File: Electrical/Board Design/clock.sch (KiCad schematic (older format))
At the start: 40 parts, among them CON1 AVR-ISP-6, IC1 ATTINY84A-SS, Q1 FET_N, Q2 FET_P, SW1 SPST, U1 MCP1624, X1 CRYSTAL 32.768kHz

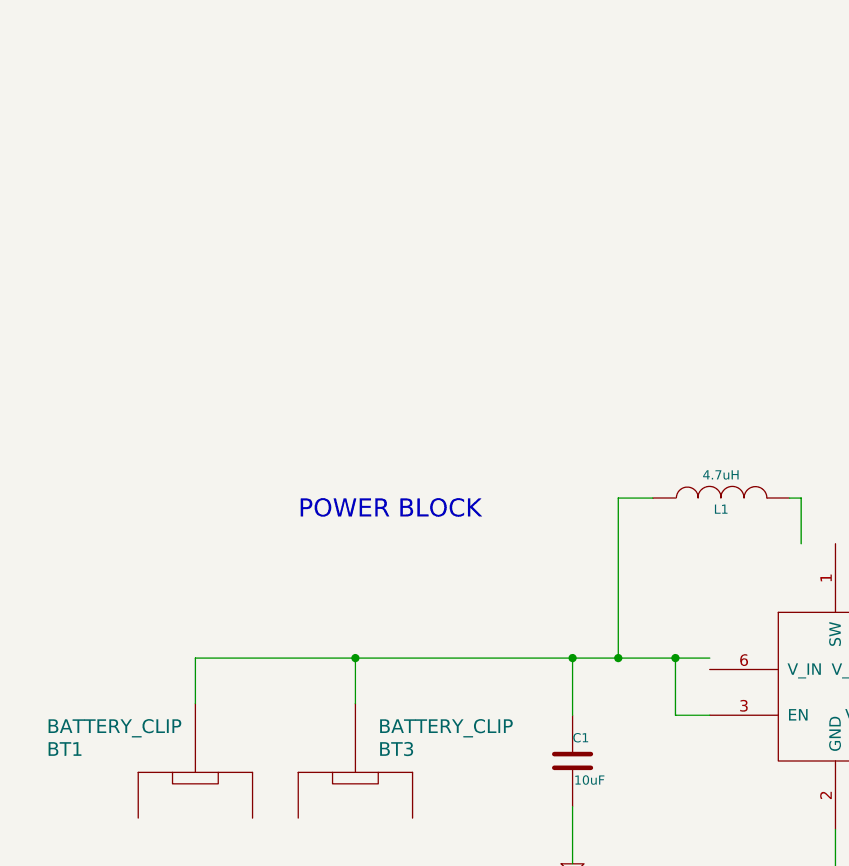
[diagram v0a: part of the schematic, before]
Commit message: added LDO to schematic and board
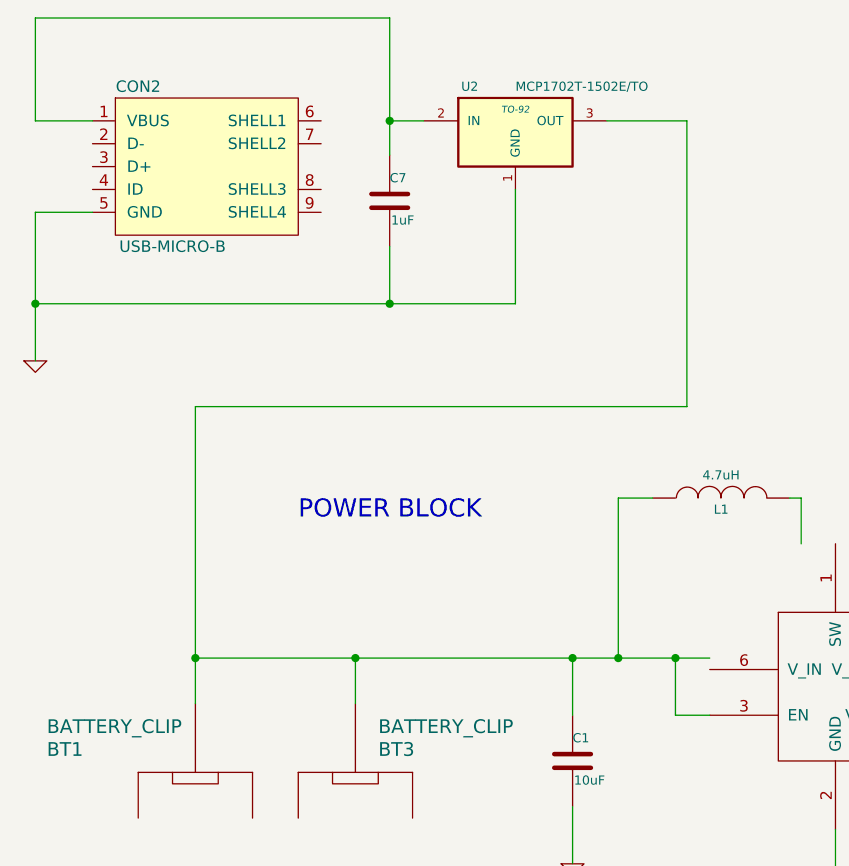
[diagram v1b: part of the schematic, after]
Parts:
- added C7: 1uF, ~, symbol C
- added CON2: USB-MICRO-B, symbol USB-MICRO-B
- added U2: MCP1702T-1502E/TO, TO-92, symbol MCP1702T-1502E/TO
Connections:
- wire segments 113 -> 126
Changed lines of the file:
@@
 Sheet 1 1
 Title ""
-Date "25 jul 2014"
+Date "4 jan 2015"
 Rev ""
 Comp ""
@@
 $EndDescr
 $Comp
-L GND #PWR01
+L GND #PWR19
 U 1 1 5336447B
 P 10600 5100
-F 0 "#PWR01" H 10600 5100 30  0001 C CNN
+F 0 "#PWR19" H 10600 5100 30  0001 C CNN
 F 1 "GND" H 10600 5030 30  0001 C CNN
 F 2 "" H 10600 5100 60  0000 C CNN
@@
 $EndComp
 $Comp
-L GND #PWR02
+L GND #PWR18
 U 1 1 53364495
 P 9400 5400
-F 0 "#PWR02" H 9400 5400 30  0001 C CNN
+F 0 "#PWR18" H 9400 5400 30  0001 C CNN
 F 1 "GND" H 9400 5330 30  0001 C CNN
 F 2 "" H 9400 5400 60  0000 C CNN
@@
 $EndComp
 $Comp
-L GND #PWR03
+L GND #PWR15
 U 1 1 5336449B
 P 8400 5000
-F 0 "#PWR03" H 8400 5000 30  0001 C CNN
+F 0 "#PWR15" H 8400 5000 30  0001 C CNN
 F 1 "GND" H 8400 4930 30  0001 C CNN
 F 2 "" H 8400 5000 60  0000 C CNN
@@
 $EndComp
 $Comp
-L VCC #PWR04
+L VCC #PWR17
 U 1 1 533644C9
 P 9350 3400
-F 0 "#PWR04" H 9350 3500 30  0001 C CNN
+F 0 "#PWR17" H 9350 3500 30  0001 C CNN
 F 1 "VCC" H 9350 3500 30  0000 C CNN
 F 2 "" H 9350 3400 60  0000 C CNN
@@
 $EndComp
 $Comp
-L GND #PWR05
+L GND #PWR16
 U 1 1 53364820
 P 8950 8350
-F 0 "#PWR05" H 8950 8350 30  0001 C CNN
+F 0 "#PWR16" H 8950 8350 30  0001 C CNN
 F 1 "GND" H 8950 8280 30  0001 C CNN
 F 2 "" H 8950 8350 60  0000 C CNN
@@
 $EndComp
 $Comp
-L GND #PWR06
+L GND #PWR14
 U 1 1 53364C53
 P 7300 9250
-F 0 "#PWR06" H 7300 9250 30  0001 C CNN
+F 0 "#PWR14" H 7300 9250 30  0001 C CNN
 F 1 "GND" H 7300 9180 30  0001 C CNN
 F 2 "" H 7300 9250 60  0000 C CNN
@@
 $EndComp
 $Comp
-L GND #PWR07
+L GND #PWR11
 U 1 1 53364C59
 P 6300 9250
-F 0 "#PWR07" H 6300 9250 30  0001 C CNN
+F 0 "#PWR11" H 6300 9250 30  0001 C CNN
 F 1 "GND" H 6300 9180 30  0001 C CNN
 F 2 "" H 6300 9250 60  0000 C CNN
@@
 $EndComp
 $Comp
-L GND #PWR08
+L GND #PWR23
 U 1 1 53365252
 P 12800 7350
-F 0 "#PWR08" H 12800 7350 30  0001 C CNN
+F 0 "#PWR23" H 12800 7350 30  0001 C CNN
 F 1 "GND" H 12800 7280 30  0001 C CNN
 F 2 "" H 12800 7350 60  0000 C CNN
@@
 $EndComp
 $Comp
-L GND #PWR09
+L GND #PWR24
 U 1 1 53365258
 P 12800 7650
-F 0 "#PWR09" H 12800 7650 30  0001 C CNN
+F 0 "#PWR24" H 12800 7650 30  0001 C CNN
 F 1 "GND" H 12800 7580 30  0001 C CNN
 F 2 "" H 12800 7650 60  0000 C CNN
@@
 $EndComp
 $Comp
-L GND #PWR010
+L GND #PWR21
 U 1 1 53365387
 P 12200 8650
-F 0 "#PWR010" H 12200 8650 30  0001 C CNN
+F 0 "#PWR21" H 12200 8650 30  0001 C CNN
 F 1 "GND" H 12200 8580 30  0001 C CNN
 F 2 "" H 12200 8650 60  0000 C CNN
@@
 LIGHTS / BUZZER (EXTRA)
 $Comp
-L VCC #PWR011
+L VCC #PWR3
 U 1 1 53365427
 P 2150 6100
-F 0 "#PWR011" H 2150 6200 30  0001 C CNN
+F 0 "#PWR3" H 2150 6200 30  0001 C CNN
 F 1 "VCC" H 2150 6200 30  0000 C CNN
 F 2 "" H 2150 6100 60  0000 C CNN
@@
 $EndComp
 $Comp
-L GND #PWR012
+L GND #PWR4
 U 1 1 5336542D
 P 2150 7950
-F 0 "#PWR012" H 2150 7950 30  0001 C CNN
+F 0 "#PWR4" H 2150 7950 30  0001 C CNN
 F 1 "GND" H 2150 7880 30  0001 C CNN
 F 2 "" H 2150 7950 60  0000 C CNN
@@
 MODE SELECT POWER
 $Comp
-L GND #PWR013
+L GND #PWR7
 U 1 1 5373C40E
 P 4600 4600
-F 0 "#PWR013" H 4600 4600 30  0001 C CNN
+F 0 "#PWR7" H 4600 4600 30  0001 C CNN
 F 1 "GND" H 4600 4530 30  0001 C CNN
 F 2 "" H 4600 4600 60  0000 C CNN
@@
 $EndComp
 $Comp
-L GND #PWR014
+L GND #PWR12
 U 1 1 5373C5A4
 P 6400 4650
-F 0 "#PWR014" H 6400 4650 30  0001 C CNN
+F 0 "#PWR12" H 6400 4650 30  0001 C CNN
 F 1 "GND" H 6400 4580 30  0001 C CNN
 F 2 "" H 6400 4650 60  0000 C CNN
@@
 $EndComp
 $Comp
-L VCC #PWR015
+L VCC #PWR13
 U 1 1 5373CA73
 P 7000 3600
-F 0 "#PWR015" H 7000 3700 30  0001 C CNN
+F 0 "#PWR13" H 7000 3700 30  0001 C CNN
 F 1 "VCC" H 7000 3700 30  0000 C CNN
 F 2 "" H 7000 3600 60  0000 C CNN
@@
 $EndComp
 $Comp
-L GND #PWR016
+L GND #PWR10
 U 1 1 5373CA80
 P 5800 5350
-F 0 "#PWR016" H 5800 5350 30  0001 C CNN
+F 0 "#PWR10" H 5800 5350 30  0001 C CNN
 F 1 "GND" H 5800 5280 30  0001 C CNN
 F 2 "" H 5800 5350 60  0000 C CNN
@@
 $EndComp
 $Comp
-L GND #PWR017
+L GND #PWR6
 U 1 1 5373D15F
 P 3450 4500
-F 0 "#PWR017" H 3450 4500 30  0001 C CNN
+F 0 "#PWR6" H 3450 4500 30  0001 C CNN
 F 1 "GND" H 3450 4430 30  0001 C CNN
 F 2 "" H 3450 4500 60  0000 C CNN
@@
 $EndComp
 $Comp
-L GND #PWR018
+L GND #PWR5
 U 1 1 5373D423
 P 2500 5250
-F 0 "#PWR018" H 2500 5250 30  0001 C CNN
+F 0 "#PWR5" H 2500 5250 30  0001 C CNN
 F 1 "GND" H 2500 5180 30  0001 C CNN
 F 2 "" H 2500 5250 60  0000 C CNN
@@
 $EndComp
 $Comp
-L GND #PWR019
+L GND #PWR2
 U 1 1 5373D429
 P 1800 5250
-F 0 "#PWR019" H 1800 5250 30  0001 C CNN
+F 0 "#PWR2" H 1800 5250 30  0001 C CNN
 F 1 "GND" H 1800 5180 30  0001 C CNN
 F 2 "" H 1800 5250 60  0000 C CNN
@@
 	3450 4250 3450 4500
 Wire Wire Line
-	1800 3800 1800 3600
+	1800 2500 1800 3800
 Wire Wire Line
 	2500 3800 2500 3600
@@
 Connection ~ 12700 3300
 $Comp
-L GND #PWR020
+L GND #PWR22
 U 1 1 537512F1
 P 12700 6100
-F 0 "#PWR020" H 12700 6100 30  0001 C CNN
+F 0 "#PWR22" H 12700 6100 30  0001 C CNN
 F 1 "GND" H 12700 6030 30  0001 C CNN
 F 2 "" H 12700 6100 60  0000 C CNN
@@
 	15150 5900 15150 6100
 $Comp
-L GND #PWR021
+L GND #PWR25
 U 1 1 537516B3
 P 13750 6100
-F 0 "#PWR021" H 13750 6100 30  0001 C CNN
+F 0 "#PWR25" H 13750 6100 30  0001 C CNN
 F 1 "GND" H 13750 6030 30  0001 C CNN
 F 2 "" H 13750 6100 60  0000 C CNN
@@
 $EndComp
 $Comp
-L GND #PWR022
+L GND #PWR26
 U 1 1 537516B9
 P 15150 6100
-F 0 "#PWR022" H 15150 6100 30  0001 C CNN
+F 0 "#PWR26" H 15150 6100 30  0001 C CNN
 F 1 "GND" H 15150 6030 30  0001 C CNN
 F 2 "" H 15150 6100 60  0000 C CNN
@@
 	11950 8750 11950 8850
 $Comp
-L GND #PWR023
+L GND #PWR20
 U 1 1 53764BAE
 P 11950 8850
-F 0 "#PWR023" H 11950 8850 30  0001 C CNN
+F 0 "#PWR20" H 11950 8850 30  0001 C CNN
 F 1 "GND" H 11950 8780 30  0001 C CNN
 F 2 "" H 11950 8850 60  0000 C CNN
@@
 	5700 9750 5700 9850
 $Comp
-L GND #PWR024
+L GND #PWR9
 U 1 1 53777472
 P 5700 9850
-F 0 "#PWR024" H 5700 9850 30  0001 C CNN
+F 0 "#PWR9" H 5700 9850 30  0001 C CNN
 F 1 "GND" H 5700 9780 30  0001 C CNN
 F 2 "" H 5700 9850 60  0000 C CNN
@@
 $EndComp
 $Comp
-L VCC #PWR025
+L VCC #PWR8
 U 1 1 5377747A
 P 5700 9450
-F 0 "#PWR025" H 5700 9550 30  0001 C CNN
+F 0 "#PWR8" H 5700 9550 30  0001 C CNN
 F 1 "VCC" H 5700 9550 30  0000 C CNN
 F 2 "" H 5700 9450 60  0000 C CNN
@@
 Wire Wire Line
 	7550 4200 7900 4200
+$Comp
+L USB-MICRO-B CON2
+U 1 1 54A87A25
+P 1850 1450
+F 0 "CON2" H 1550 1800 50  0000 C CNN
+F 1 "USB-MICRO-B" H 1700 1100 50  0000 C CNN
+F 2 "" H 1850 1350 50  0000 C CNN
+F 3 "" H 1850 1350 50  0000 C CNN
+	1    1850 1450
+	1    0    0    -1
+$EndComp
+$Comp
+L MCP1702T-1502E/TO U2
+U 1 1 54A87F96
+P 3200 1300
+F 0 "U2" H 3000 1500 40  0000 C CNN
+F 1 "MCP1702T-1502E/TO" H 3200 1500 40  0000 L CNN
+F 2 "TO-92" H 3200 1400 30  0000 C CIN
+F 3 "~" H 3200 1300 60  0000 C CNN
+	1    3200 1300
+	1    0    0    -1
+$EndComp
+Wire Wire Line
+	2650 1250 2800 1250
+Wire Wire Line
+	3200 2050 3200 1550
+Wire Wire Line
+	3600 1250 3950 1250
+Wire Wire Line
+	3950 1250 3950 2500
+Wire Wire Line
+	3950 2500 1800 2500
+Connection ~ 1800 3600
+Wire Wire Line
+	2650 800  2650 1400
+Wire Wire Line
+	1100 800  2650 800
+Wire Wire Line
+	1100 1250 1100 800
+Connection ~ 1100 2050
+$Comp
+L GND #PWR1
+U 1 1 54A88164
+P 1100 2300
+F 0 "#PWR1" H 1100 2300 30  0001 C CNN
+F 1 "GND" H 1100 2230 30  0001 C CNN
+F 2 "" H 1100 2300 60  0000 C CNN
+F 3 "" H 1100 2300 60  0000 C CNN
+	1    1100 2300
+	1    0    0    -1
+$EndComp
+Wire Wire Line
+	1100 2050 3200 2050
+Wire Wire Line
+	1100 1650 1100 2300
+Wire Wire Line
+	1350 1650 1100 1650
+Wire Wire Line
+	1350 1250 1100 1250
+$Comp
+L C C7
+U 1 1 54A89CEC
+P 2650 1600
+F 0 "C7" H 2650 1700 40  0000 L CNN
+F 1 "1uF" H 2656 1515 40  0000 L CNN
+F 2 "~" H 2688 1450 30  0000 C CNN
+F 3 "~" H 2650 1600 60  0000 C CNN
+	1    2650 1600
+	1    0    0    -1
+$EndComp
+Connection ~ 2650 1250
+Wire Wire Line
+	2650 1800 2650 2050
+Connection ~ 2650 2050
 $EndSCHEMATC

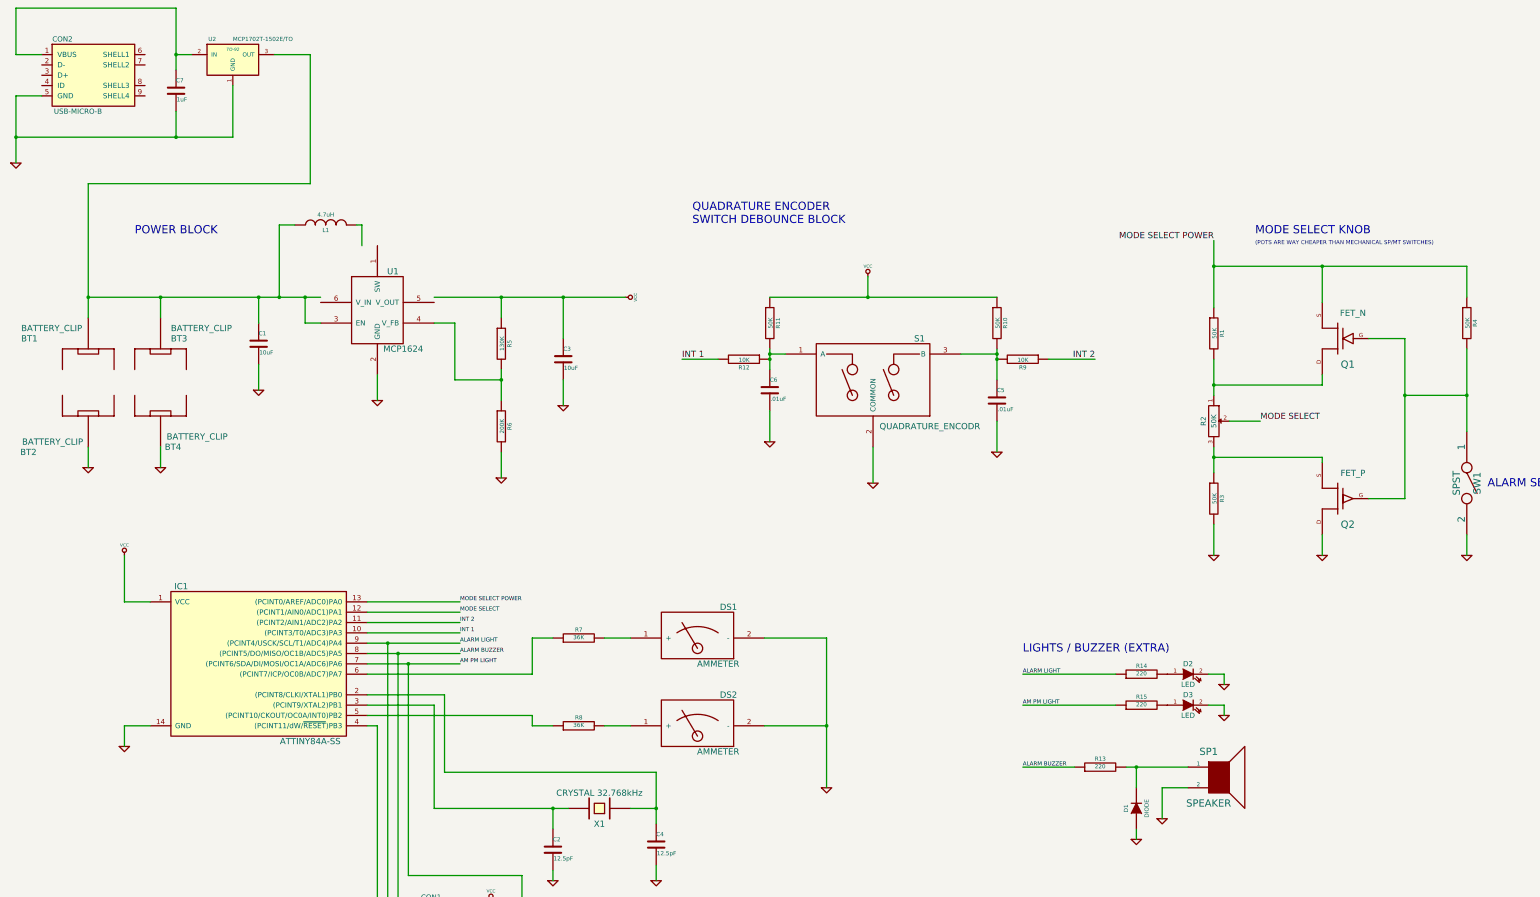
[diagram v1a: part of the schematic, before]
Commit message: schematic back in old version of kicad
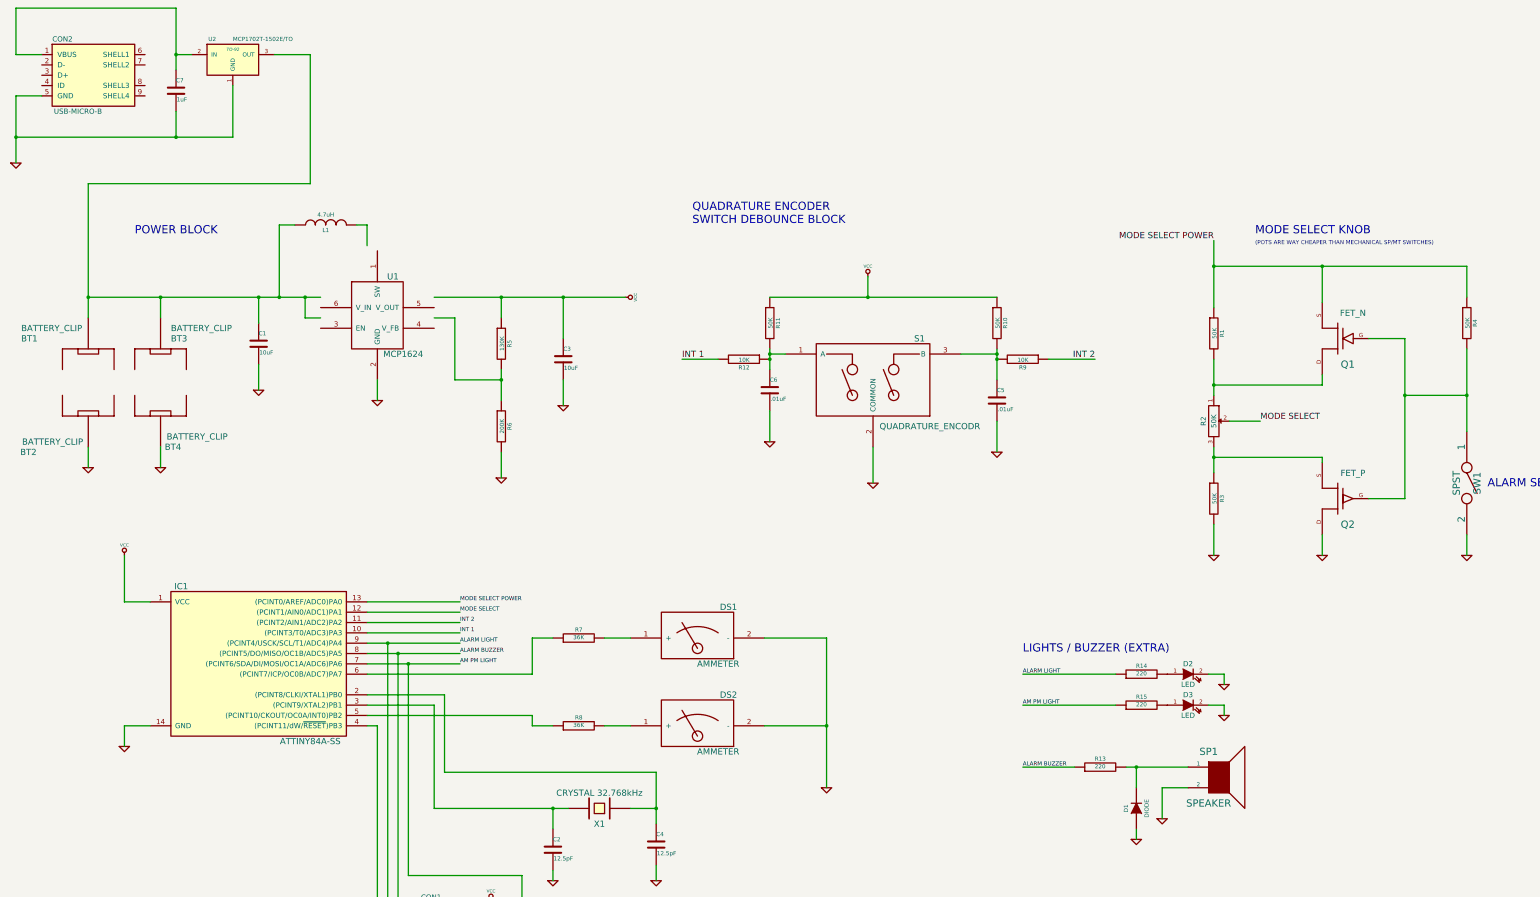
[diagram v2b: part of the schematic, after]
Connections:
- wire segments 126 -> 155
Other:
- moved on the sheet: U1
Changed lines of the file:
@@
 LIBS:clock_schematic_library
 LIBS:clock-cache
-EELAYER 27 0
+EELAYER 25 0
 EELAYER END
 $Descr USLedger 17000 11000
@@
 L MCP1624 U1
 U 1 1 5373C97A
-P 4600 3750
-F 0 "U1" H 4750 4150 60  0000 C CNN
-F 1 "MCP1624" H 4850 3400 60  0000 C CNN
-F 2 "~" H 4550 4250 60  0000 C CNN
-F 3 "~" H 4550 4250 60  0000 C CNN
-	1    4600 3750
+P 4600 3800
+F 0 "U1" H 4750 4200 60  0000 C CNN
+F 1 "MCP1624" H 4850 3450 60  0000 C CNN
+F 2 "~" H 4550 4300 60  0000 C CNN
+F 3 "~" H 4550 4300 60  0000 C CNN
+	1    4600 3800
 	1    0    0    -1
 $EndComp
@@
 $EndComp
 Wire Wire Line
-	8400 3600 10600 3600
-Wire Wire Line
-	8400 4100 8400 4300
-Wire Wire Line
-	10600 4100 10600 4400
+	8400 3600 9350 3600
+Wire Wire Line
+	9350 3600 10600 3600
+Wire Wire Line
+	8400 4100 8400 4150
+Wire Wire Line
+	8400 4150 8400 4200
+Wire Wire Line
+	8400 4200 8400 4300
+Wire Wire Line
+	10600 4100 10600 4150
+Wire Wire Line
+	10600 4150 10600 4200
+Wire Wire Line
+	10600 4200 10600 4400
 Connection ~ 8400 4150
 Connection ~ 10600 4200
@@
 	5150 7550 5150 8550
 Wire Wire Line
-	5150 8550 6450 8550
-Wire Wire Line
-	7300 8200 7300 8700
+	5150 8550 6300 8550
+Wire Wire Line
+	6300 8550 6450 8550
+Wire Wire Line
+	7300 8200 7300 8550
+Wire Wire Line
+	7300 8550 7300 8700
 Wire Wire Line
 	6300 8550 6300 8750
@@
 	4500 6650 5400 6650
 Wire Wire Line
-	4500 6950 5400 6950
+	4500 6950 4700 6950
+Wire Wire Line
+	4700 6950 5400 6950
 Wire Wire Line
 	10850 7250 11750 7250
@@
 	4900 9200 4900 7150
 Wire Wire Line
-	8950 6900 8950 8350
+	8950 6900 8950 7750
+Wire Wire Line
+	8950 7750 8950 8350
 Wire Wire Line
 	4500 6550 5400 6550
@@
 Connection ~ 4900 7150
 Wire Wire Line
-	4500 7050 5400 7050
-Wire Wire Line
-	4500 7150 5400 7150
-Wire Wire Line
-	4600 4350 4600 4600
-Wire Wire Line
-	5150 3600 7000 3600
-Wire Wire Line
-	5800 4300 5800 4600
+	4500 7050 4800 7050
+Wire Wire Line
+	4800 7050 5400 7050
+Wire Wire Line
+	4500 7150 4900 7150
+Wire Wire Line
+	4900 7150 5400 7150
+Wire Wire Line
+	4600 4400 4600 4600
+Wire Wire Line
+	5150 3600 5800 3600
+Wire Wire Line
+	5800 3600 6400 3600
+Wire Wire Line
+	6400 3600 7000 3600
+Wire Wire Line
+	5800 4300 5800 4400
+Wire Wire Line
+	5800 4400 5800 4600
 Wire Wire Line
 	6400 4400 6400 4650
 Wire Wire Line
-	5150 3850 5350 3850
-Wire Wire Line
-	5350 3850 5350 4400
+	5150 3800 5350 3800
+Wire Wire Line
+	5350 3800 5350 4400
 Wire Wire Line
 	5350 4400 5800 4400
@@
 	5800 5100 5800 5350
 Wire Wire Line
-	1800 3600 4050 3600
-Wire Wire Line
-	3900 3600 3900 3850
-Wire Wire Line
-	3900 3850 4050 3850
+	1800 3600 2500 3600
+Wire Wire Line
+	2500 3600 3450 3600
+Wire Wire Line
+	3450 3600 3650 3600
+Wire Wire Line
+	3650 3600 3900 3600
+Wire Wire Line
+	3900 3600 4050 3600
+Wire Wire Line
+	3900 3600 3900 3800
+Wire Wire Line
+	3900 3800 4050 3800
 Wire Wire Line
 	3650 3600 3650 2900
@@
 Connection ~ 3900 3600
 Wire Wire Line
-	4400 2900 4450 2900
-Wire Wire Line
-	4450 2900 4450 3100
+	4400 2900 4500 2900
+Wire Wire Line
+	4500 2900 4500 3100
 Connection ~ 3650 3600
 Wire Wire Line
@@
 	3450 4250 3450 4500
 Wire Wire Line
-	1800 2500 1800 3800
+	1800 2500 1800 3600
+Wire Wire Line
+	1800 3600 1800 3800
 Wire Wire Line
 	2500 3800 2500 3600
@@
 	6100 7750 6300 7750
 Wire Wire Line
-	12700 4200 12700 4550
-Wire Wire Line
-	12700 5050 12700 5300
+	12700 4200 12700 4450
+Wire Wire Line
+	12700 4450 12700 4550
+Wire Wire Line
+	12700 5050 12700 5150
+Wire Wire Line
+	12700 5150 12700 5300
 Wire Wire Line
 	12850 4800 13150 4800
 Wire Wire Line
-	12700 3050 12700 3700
-Wire Wire Line
-	15150 4100 15150 4900
+	12700 3050 12700 3300
+Wire Wire Line
+	12700 3300 12700 3700
+Wire Wire Line
+	15150 4100 15150 4550
+Wire Wire Line
+	15150 4550 15150 4900
 Wire Wire Line
 	15150 4550 14550 4550
 Wire Wire Line
-	14550 4000 14550 5550
+	14550 4000 14550 4550
+Wire Wire Line
+	14550 4550 14550 5550
 Wire Wire Line
 	14550 4000 14200 4000
@@
 	15150 3300 15150 3600
 Wire Wire Line
-	12700 3300 15150 3300
+	12700 3300 13750 3300
+Wire Wire Line
+	13750 3300 15150 3300
 Connection ~ 12700 3300
 $Comp
@@
 $EndComp
 Wire Wire Line
-	11850 8150 12450 8150
+	11850 8150 11950 8150
+Wire Wire Line
+	11950 8150 12450 8150
 Wire Wire Line
 	11350 8150 10850 8150
@@
 Connection ~ 1800 3600
 Wire Wire Line
-	2650 800  2650 1400
+	2650 800  2650 1250
+Wire Wire Line
+	2650 1250 2650 1400
 Wire Wire Line
 	1100 800  2650 800
@@
 $EndComp
 Wire Wire Line
-	1100 2050 3200 2050
-Wire Wire Line
-	1100 1650 1100 2300
+	1100 2050 2650 2050
+Wire Wire Line
+	2650 2050 3200 2050
+Wire Wire Line
+	1100 1650 1100 2050
+Wire Wire Line
+	1100 2050 1100 2300
 Wire Wire Line
 	1350 1650 1100 1650

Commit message: electrical design updates
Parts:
- added P1: CONN_6, symbol CONN_6
- added P2, P3: CONN_2, symbol CONN_2
- R1, R2, R3, R4: value 50K -> 100K
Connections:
- net labels added: BATTERY POWER, HOURS, MINUTES
- wire segments 155 -> 142
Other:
- note added: "POWER FOR LIGHTING"
- note added: "TEST PORT BLOCK"
- moved on the sheet: U1
